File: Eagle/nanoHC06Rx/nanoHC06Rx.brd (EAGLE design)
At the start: 99.1 x 85.6 mm, 53 parts, among them J10 Relay, J14 Relay, J17 Relay, J2 Relay, J20 Pixel, J22 IR Rx, J33 Relay, Q1 2N5088, Q2 2N5088, X1 53047-11

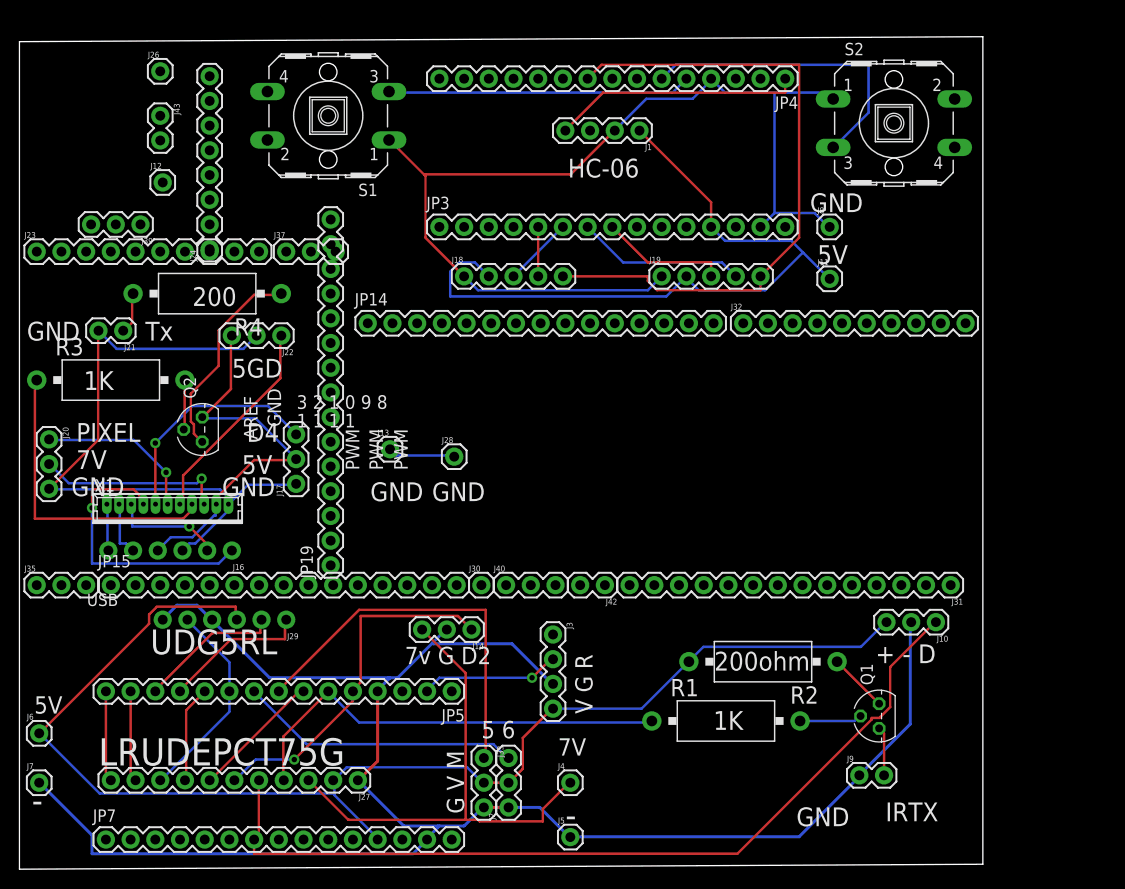
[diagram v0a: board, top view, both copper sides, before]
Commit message: Bind HC05 and HC06
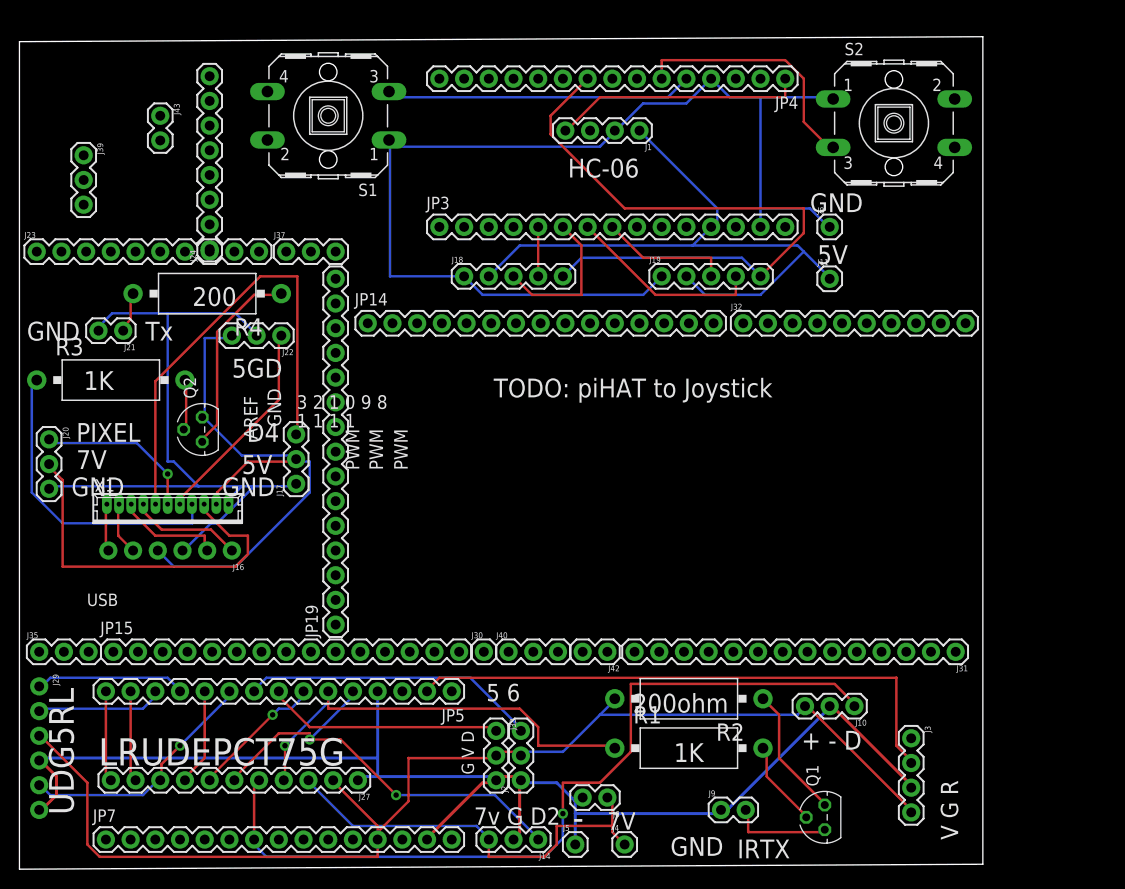
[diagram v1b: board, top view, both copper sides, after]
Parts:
- removed J12, J13, J26, J28, J7: (no value), SparkFun-Connectors:1X01
- J6: device SparkFun-Connectors:1X01 -> SparkFun-Connectors:1X02
- moved J6 58.8 mm to (60.5, 7.37), turned to 180 degrees
- moved J3 38.3 mm to (91.7, 13.5)
- moved J29 26.3 mm to (2.03, 18.8), turned to 270 degrees
- moved J14 22.7 mm to (53.3, 3.05)
- moved J9 14.7 mm to (72.1, 6.10)
- moved J10 12.0 mm to (85.9, 16.8)
- moved Q1 11.8 mm to (82.8, 5.33)
- moved J39 9.20 mm to (6.60, 73.4), turned to 270 degrees
- moved R2 8.52 mm to (68.8, 17.5)
- moved J4 8.46 mm to (62.2, 2.54)
- moved J31 6.88 mm to (96.3, 22.4)
- moved J30 6.86 mm to (47.8, 22.4)
- moved J35 6.86 mm to (2.03, 22.4)
- moved J40 6.86 mm to (50.3, 22.4)
- moved J42 6.86 mm to (60.5, 22.4)
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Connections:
- removed net 7V_B: J26.1
- removed net GND_B: J13.1, J28.1
- removed net VCC_B: J12.1
- net 7.4V: now also J6.1
- net GND: now also J6.2; no longer J7.1
- net VCC: no longer J6.1
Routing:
- net GND: track 183.8 -> 139.7 mm
- net D0: track 14.4 -> 58.3 mm, vias 1 -> 0
- net RELAY_C: track 23.6 -> 48.0 mm, vias 1 -> 0
- net 7.4V_C: track 19.4 -> 38.8 mm, vias 1 -> 0
- net DOWN_C: track 28.8 -> 11.5 mm, vias 1 -> 0
- net 5V_C: track 40.3 -> 57.4 mm
- net D5: track 40.2 -> 24.4 mm
- net VCC: track 135.3 -> 123.7 mm
- net 7.4V: track 52.5 -> 43.7 mm
- net D2: track 36.6 -> 45.1 mm, vias 1 -> 2
- net A2_D: track 7.18 -> 15.5 mm
- net GND_D: track 106.5 -> 114.8 mm
- net N$3: track 6.11 -> 13.5 mm
- net GND_B: track 6.93 -> 0.00 mm
- net D3_D: track 31.9 -> 25.8 mm
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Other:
- board text added: "G V D"
- board text added: "TODO: piHAT to Joystick"
- board text removed: "G V M"

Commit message: eagle
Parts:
- removed J21: (no value), SparkFun-Connectors:1X02
- removed J22: IR Rx, SparkFun-Connectors:1X03
- removed Q2: 2N5088, transistor-npn:TO92
- removed R3: 1K, resistor-power:CA0001
- removed R4: 200ohm, resistor-power:CA0001
- removed X1: 53047-11, con-molex:53047-11
- added C1: 10uF, SparkFun-Capacitors:CPOL-RADIAL-2.5MM-5MM-KIT
- added J12, J25, J26, J7: (no value), SparkFun-Connectors:1X06_NO_SILK
- added J13, J15: (no value), SparkFun-Connectors:1X08
- added J28: (no value), SparkFun-Connectors:1X01
- added J34: (no value), SparkFun-Connectors:1X04
- added PROG, PROG1, PROG2: (no value), SparkFun-Connectors:1X02
- added S3, S4: (no value), switch-omron:B3F-40XX
- added U$1: V_REG_LD1117VXX, SparkFun-IC-Power:78XXL
- J16: value (none) -> Relay; device SparkFun-Connectors:1X06_NO_SILK -> SparkFun-Connectors:1X03
- J20: value Pixel -> (none); device SparkFun-Connectors:1X03 -> SparkFun-Connectors:1X06_NO_SILK
- moved J8 64.4 mm to (19.1, 69.8)
- moved J11 64.3 mm to (19.1, 63.5)
- moved JP19 25.1 mm to (7.37, 25.1)
- moved J43 16.0 mm to (14.7, 61.5)
- moved J20 9.11 mm to (11.4, 40.6)
- moved J37 7.41 mm to (28.2, 56.1)
- moved J23 7.38 mm to (2.29, 56.1)
- moved J16 6.78 mm to (28.4, 34.3), turned to 90 degrees
- moved J24 4.83 mm to (14.7, 64.0)
- moved J17 3.06 mm to (25.4, 39.4), turned to 270 degrees
- moved JP3 2.54 mm to (40.6, 66.0)
- moved JP4 2.54 mm to (76.2, 81.3)
- moved S2 1.80 mm to (90.2, 78.5)
- moved S1 1.70 mm to (30.2, 78.2)
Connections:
- removed net 5V_C: J16.4, J17.2, J22.3, Q2.1, X1.2
- removed net 7.4V_C: J20.2, X1.3
- removed net DOWN_C: J16.1, X1.8
- removed net GND_C: J16.3, J17.1, J20.3, J21.2, J22.2, X1.1
- removed net LEFT_C: J16.6, X1.11
- removed net N$2: Q2.2, R3.2
- removed net N$4: Q2.3, R4.1
- removed net PIXEL_C: J20.1, X1.6
- removed net RELAY_C: J17.3, X1.7
- removed net RIGHT_C: J16.5, X1.10
- removed net RXIR_C: J22.1, X1.5
- removed net TXIR_C: R3.1, X1.4
- removed net TX_C: J21.1, R4.2
- removed net UP_C: J16.2, X1.9
- new net 3.3V_B: C1.1, J13.8, PROG1.1, PROG1.2, U$1.GND
- new net 5V_B: J16.2, J17.2, J20.3, J34.1, PROG2.1, U$1.OUT
- new net D4_D: JP4.7, S3.3
- new net D5_D: JP4.8, S4.3
- new net GND_B: C1.2, J13.1, J16.1, J17.3, J20.4, J20.6, J26.1, J26.2, J26.3, J26.4, J26.5, J26.6, J34.2, J7.6, U$1.IN
- new net GPIO02_B: J12.5, J15.7, J20.5
- new net GPIO04_B: J12.6, J15.8
- new net GPIO12_B: J12.1, J15.3, J17.1
- new net GPIO13_B: J12.2, J15.4
- new net GPIO14_B: J12.4, J15.6, J20.1
- new net GPIO15_B: J12.3, J15.5, J20.2
- new net GPIO16_B: J13.7, J16.3, J28.1
- new net PROG1: J13.5, PROG.1
- new net PROG2: J13.6, PROG.2
- new net UOR: J13.3, J34.3, J7.3
- new net UOT: J13.2, J7.2
- new net VCC_B: J15.1, J25.1, J25.2, J25.3, J25.4, J25.5, J25.6, J7.4, PROG2.2
- net GND_D: now also S3.1, S4.1
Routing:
- net UOR: track 0.00 -> 152.1 mm
- net GND_B: track 0.00 -> 130.2 mm
- net 5V_B: track 0.00 -> 114.2 mm
- net GPIO14_B: track 0.00 -> 101.0 mm
- net VCC_B: track 0.00 -> 82.1 mm
- net GPIO15_B: track 0.00 -> 81.2 mm, vias 0 -> 1
- net GND_C: track 75.7 -> 0.00 mm
- net GPIO02_B: track 0.00 -> 66.7 mm
- net 5V_C: track 57.4 -> 0.00 mm
- net RELAY_C: track 48.0 -> 0.00 mm
- net GPIO12_B: track 0.00 -> 41.9 mm
- net PROG2: track 0.00 -> 41.4 mm
- net D4_D: track 0.00 -> 39.3 mm
- net D2: track 45.1 -> 84.4 mm, vias 2 -> 1
- net 7.4V_C: track 38.8 -> 0.00 mm
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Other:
- board text added: "12"
- board text added: "16"
- board text added: "5V<->VCC"
- board text added: "ESP32 Cam to programmer and breakout"
- board text added: "GN"
- board text added: "GPIO02"
- board text added: "GPIO04"
- board text added: "GPIO12"
- board text added: "GPIO13"
- board text added: "GPIO14"
- board text added: "GPIO15"
- board text added: "GPIO16"
- board text added: "Program"
- board text added: "VCC"
- board text removed: "200"
- board text removed: "5GD"
- board text removed: "D4"
- board text removed: "PIXEL"
- board text removed: "TODO: piHAT to Joystick"
- board text removed: "Tx"

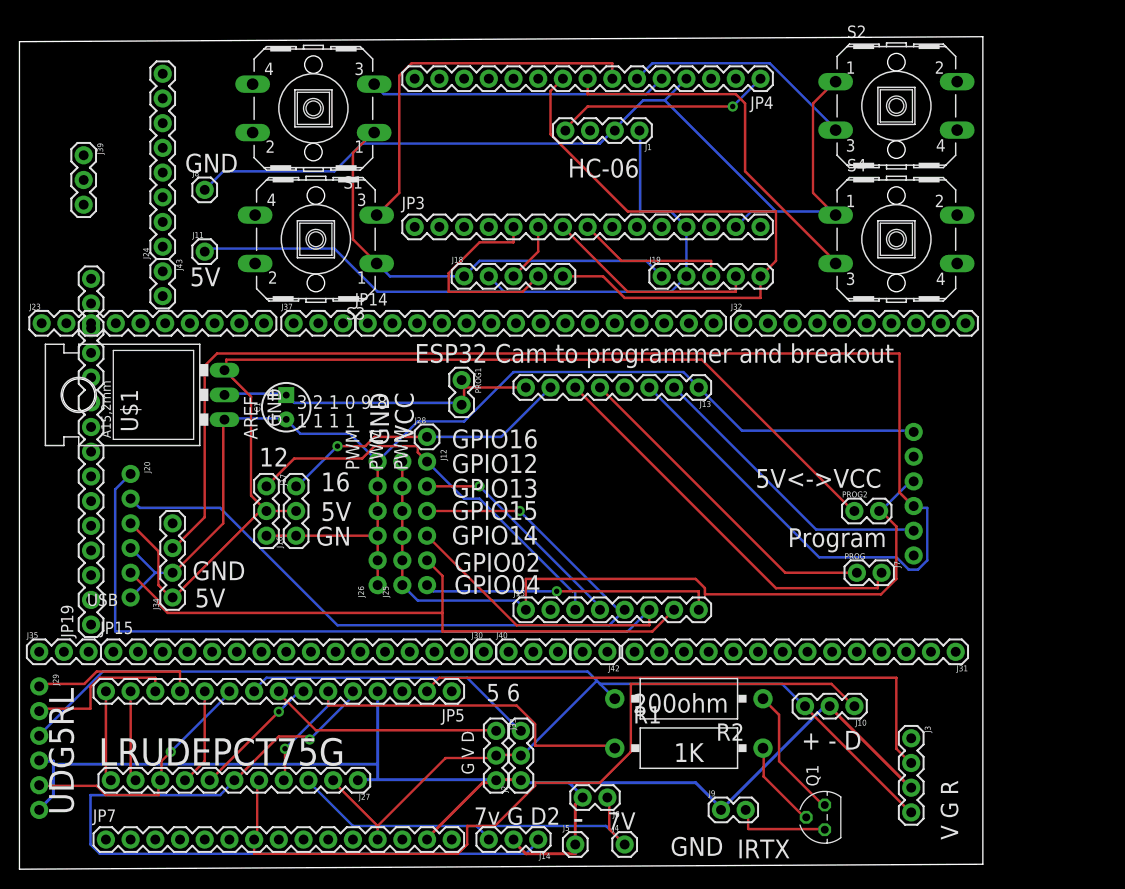
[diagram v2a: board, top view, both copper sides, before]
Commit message: esp32 bluetooth
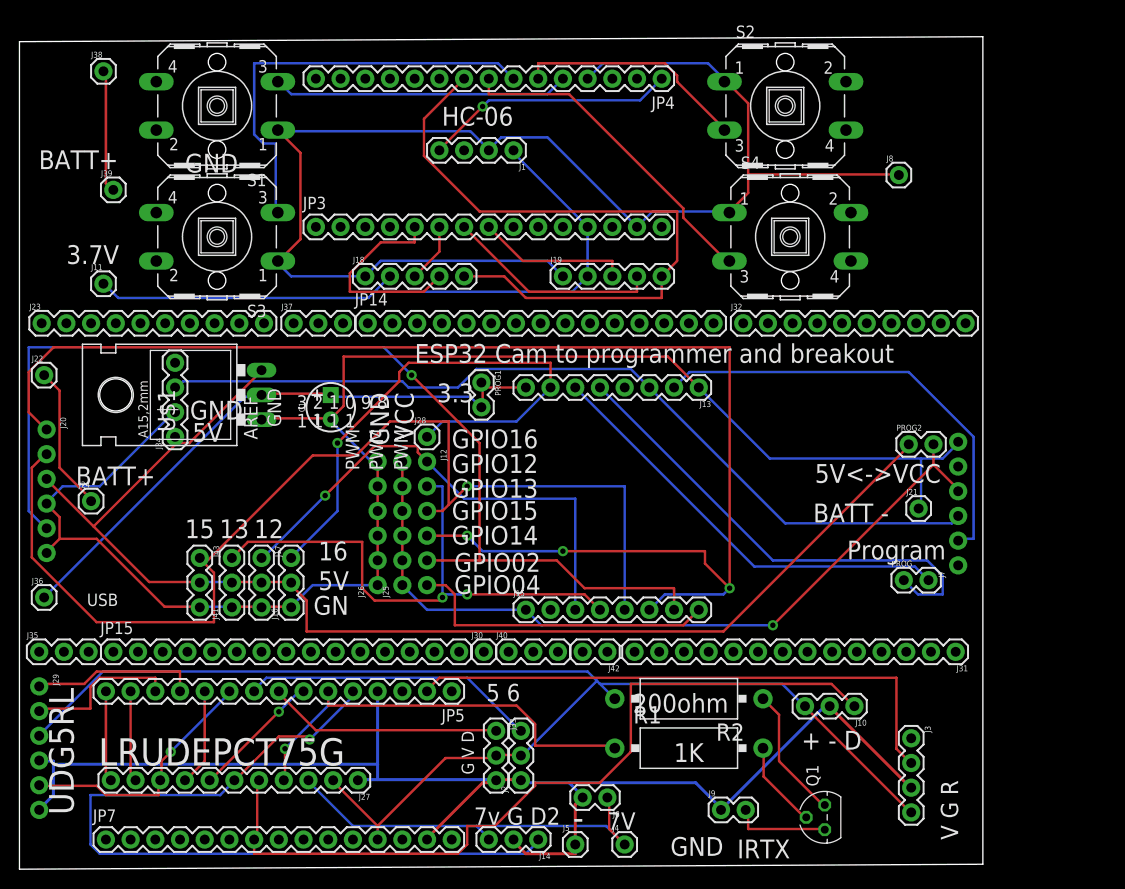
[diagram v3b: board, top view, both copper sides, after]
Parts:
- removed JP19: (no value), SparkFun-Connectors:1X15@1
- added J21, J22, J36, J38: (no value), SparkFun-Connectors:1X01
- added J41: Relay, SparkFun-Connectors:1X03
- J24: device SparkFun-Connectors:1X08 -> SparkFun-Connectors:1X01
- J39: device SparkFun-Connectors:1X03 -> SparkFun-Connectors:1X01
- J43: value (none) -> Relay; device SparkFun-Connectors:1X02 -> SparkFun-Connectors:1X03
- moved J8 71.4 mm to (90.4, 71.4)
- moved J43 29.7 mm to (18.5, 32.0)
- moved J24 27.2 mm to (7.37, 37.8), turned to 0 degrees
- moved J34 16.5 mm to (16.0, 44.5)
- moved J1 13.1 mm to (50.8, 73.9)
- moved S2 11.4 mm to (78.7, 78.5)
- moved J11 10.9 mm to (8.64, 60.2)
- moved S4 10.9 mm to (79.2, 65.0)
- moved S3 10.2 mm to (20.3, 65.0)
- moved J19 10.2 mm to (55.9, 61.0)
- moved JP3 10.2 mm to (30.5, 66.0)
- moved J18 10.2 mm to (35.6, 61.0)
- moved JP4 10.2 mm to (66.0, 81.3)
- moved S1 9.91 mm to (20.3, 78.5)
- moved J20 9.77 mm to (2.79, 45.2)
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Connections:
- new net BATT3.3V_B: J22.1, J24.1
- new net BATT_3V3_D: J38.1, J39.1
- net 3.3V_B: now also J36.1
- net 5V_B: now also J41.2, J43.2
- net GND_B: now also J21.1, J41.1, J43.3
- net GPIO13_B: now also J41.3
- net GPIO15_B: now also J43.1
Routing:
- net UOR: track 152.1 -> 88.8 mm
- net GPIO14_B: track 101.0 -> 147.8 mm, vias 0 -> 3
- net GPIO02_B: track 66.7 -> 110.7 mm, vias 0 -> 1
- net GND_B: track 130.2 -> 167.3 mm
- net GPIO13_B: track 23.2 -> 57.8 mm, vias 1 -> 2
- net GPIO15_B: track 81.2 -> 114.5 mm
- net 3.3V_B: track 34.9 -> 61.8 mm
- net GPIO16_B: track 30.4 -> 57.0 mm
- net 5V_B: track 114.2 -> 130.8 mm
- net UOT: track 30.7 -> 46.5 mm
- net PROG1: track 34.3 -> 49.8 mm
- net BATT3.3V_B: track 0.00 -> 14.9 mm
- net BATT_3V3_D: track 0.00 -> 12.7 mm
- net GPIO12_B: track 41.9 -> 51.0 mm, vias 0 -> 1
- net D6_D: track 63.5 -> 68.8 mm
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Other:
- board text added: "13"
- board text added: "15"
- board text added: "3.3"
- board text added: "3.7V"
- board text added: "BATT -"
- board text added: "BATT+"

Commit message: yo
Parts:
- added J44, J45, J46, J47: (no value), SparkFun-Connectors:1X01_2MM
- moved J21 2.81 mm to (89.7, 36.8)
- moved J24 2.03 mm to (9.40, 37.8)
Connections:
- net BATT3.3V_B: now also J46.1
- net BATT_3V3_D: now also J44.1
- net GND_B: now also J47.1
- net GND_D: now also J45.1
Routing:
- net GPIO14_B: track 147.8 -> 101.7 mm, vias 3 -> 1
- net GPIO02_B: track 110.7 -> 82.3 mm, vias 1 -> 0
- net D2: track 84.4 -> 63.6 mm, vias 1 -> 2
- net VCC: track 137.3 -> 116.9 mm, vias 0 -> 1
- net VCC_B: track 81.7 -> 102.0 mm, vias 1 -> 0
- net GPIO15_B: track 114.5 -> 133.3 mm
- net A1_D: track 21.3 -> 6.78 mm
- net GND_D: track 145.6 -> 131.3 mm
- net D4_D: track 44.5 -> 30.8 mm
- net D7: track 26.4 -> 40.0 mm, vias 1 -> 0
- net D6_D: track 68.8 -> 82.5 mm
- net GPIO16_B: track 57.0 -> 43.8 mm, vias 1 -> 0
- net D5_D: track 34.0 -> 42.6 mm
- net D5: track 24.1 -> 32.1 mm
- net D3_D: track 24.0 -> 31.7 mm
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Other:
- board text added: "Battery is alternate 3.3V source"

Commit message: Requirements
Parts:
- removed C1: 10uF, SparkFun-Capacitors:CPOL-RADIAL-2.5MM-5MM-KIT
- removed J20: (no value), SparkFun-Connectors:1X06_NO_SILK
- removed J22, J24, J28, J36: (no value), SparkFun-Connectors:1X01
- removed J27: (no value), SparkFun-Connectors:1X11
- removed J46, J47: (no value), SparkFun-Connectors:1X01_2MM
- removed PROG1: (no value), SparkFun-Connectors:1X02
- removed U$1: V_REG_LD1117VXX, SparkFun-IC-Power:78XXL
- added D1, D2, D3, D4, D5, D6: 1N5333, diode:C1702-15
- added J48: (no value), SparkFun-Connectors:1X04
- J21: device SparkFun-Connectors:1X01 -> SparkFun-Connectors:1X04
- moved J21 84.0 mm to (5.84, 42.2), turned to 90 degrees
- moved J34 20.8 mm to (5.59, 26.4)
- moved PROG2 1.52 mm to (89.9, 43.7)
- moved PROG 1.02 mm to (89.9, 29.7)
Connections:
- removed net BATT3.3V_B: J22.1, J24.1, J46.1
- new net N$2: D1.A, J16.2
- new net N$4: D2.A, J17.2
- new net N$5: D3.A, J41.2
- new net N$6: D4.A, J43.2
- new net N$7: D5.A, J2.2
- new net N$8: D6.A, J33.2
- net 3.3V_B: no longer C1.1, J36.1, PROG1.1, PROG1.2, U$1.GND
- net 5V_B: now also D1.C, D2.C, D3.C, D4.C, J21.1; no longer J16.2, J17.2, J20.3, J41.2, J43.2, U$1.OUT
- net 7.4V: no longer J27.3
- net D10_D: now also J48.1
- net D11: no longer J27.10
- net D11_D: now also J48.3
- net D12: no longer J27.11
- net D12_D: now also J48.4
- net D17: no longer J27.5
- net D2: no longer J27.6
- net D3: no longer J27.4
- net D4: no longer J27.7
- net D7: no longer J27.9
- net D8: no longer J27.8
- net GND: no longer J27.1
- net GND_B: now also J15.2, J21.2; no longer C1.2, J20.4, J20.6, J21.1, J47.1, U$1.IN
- net GPIO02_B: now also J16.3; no longer J20.5
- net GPIO04_B: now also J21.4
- net GPIO14_B: now also J43.1; no longer J20.1
- net GPIO15_B: no longer J12.3, J20.2, J43.1
- net GPIO16_B: no longer J16.3, J28.1
- net UOT: now also J21.3
- net VCC: now also D5.C, D6.C; no longer J2.2, J27.2, J33.2
- net VCC_D: now also J48.2
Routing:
- net GPIO15_B: track 133.3 -> 0.00 mm, vias 1 -> 0
- net D12_D: track 0.00 -> 110.6 mm
- net GPIO04_B: track 31.5 -> 102.7 mm, vias 1 -> 0
- net 3.3V_B: track 68.9 -> 0.00 mm
- net D10_D: track 0.00 -> 67.6 mm
- net D11_D: track 0.00 -> 63.9 mm, vias 0 -> 1
- net UOT: track 46.0 -> 102.7 mm
- net VCC_D: track 69.4 -> 113.8 mm
- net GPIO16_B: track 43.8 -> 0.00 mm
- net UOR: track 89.2 -> 128.8 mm
- net D2: track 63.6 -> 30.6 mm, vias 2 -> 0
- net GPIO02_B: track 82.3 -> 51.6 mm, vias 0 -> 2
- net D6: track 29.1 -> 57.8 mm
- net N$5: track 0.00 -> 27.2 mm
- net N$6: track 0.00 -> 25.7 mm
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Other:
- board text added: "+"
- board text added: "02"
- board text added: "14"
- board text added: "GP04"
- board text added: "RCV"
- board text added: "TX"
- board text removed: "15"
- board text removed: "16"
- board text removed: "3.3"
- board text removed: "BATT -"
- board text removed: "Battery is alternate 3.3V source"
- board text removed: "LRUDEPCT75G"

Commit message: arduino
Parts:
- added J20: Relay, SparkFun-Connectors:1X03
- moved J3 5.85 mm to (96.5, 10.2)
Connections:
- net D2: now also J20.1
- net D4: now also J3.1
- net GND: now also J20.3
- net VCC: now also J20.2
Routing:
- net D4: track 0.00 -> 78.5 mm
- net D2: track 30.6 -> 92.8 mm, vias 0 -> 2
- net D12_D: track 110.6 -> 62.8 mm
- net VCC: track 109.3 -> 142.8 mm, vias 1 -> 0
- net D6_D: track 86.8 -> 57.8 mm
- net GPIO02_B: track 51.6 -> 77.4 mm, vias 2 -> 0
- net GPIO14_B: track 86.6 -> 63.5 mm, vias 0 -> 1
- net VCC_B: track 108.5 -> 87.5 mm, vias 0 -> 1
- net D6: track 57.8 -> 40.6 mm
- net GPIO12_B: track 64.7 -> 49.6 mm, vias 2 -> 1
- net GPIO04_B: track 102.7 -> 116.1 mm
- net D0: track 58.3 -> 69.5 mm
- net UOT: track 102.7 -> 113.9 mm
- net A3_D: track 31.5 -> 21.6 mm, vias 0 -> 1
- net D5_D: track 43.3 -> 33.4 mm
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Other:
- board text added: "+ -D"
- board text added: "2VG"
- board text added: "VGR4"
- board text removed: "+ - D"
- board text removed: "V G R"
